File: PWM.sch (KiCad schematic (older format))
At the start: 28 parts

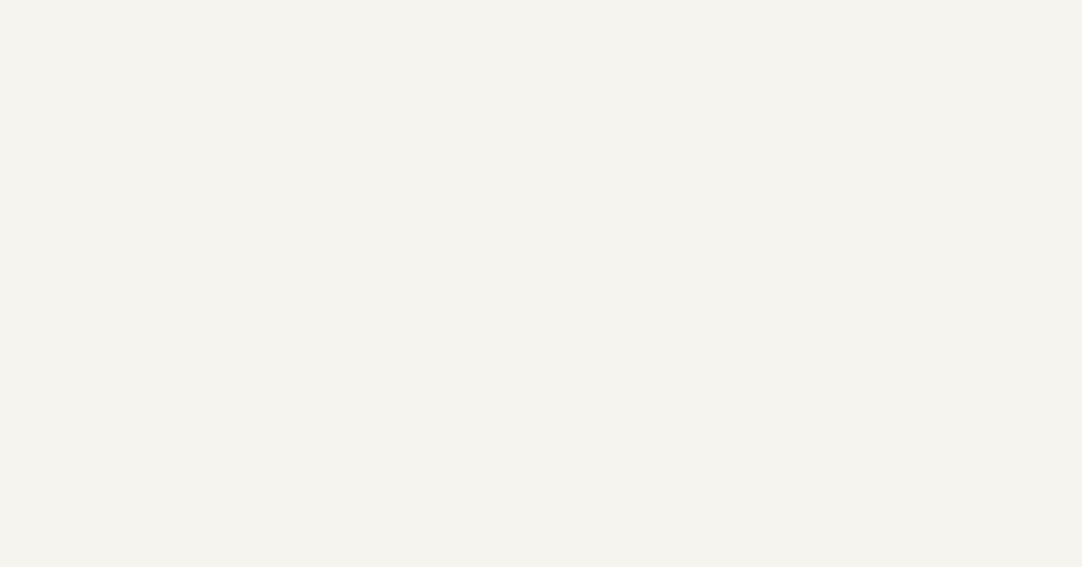
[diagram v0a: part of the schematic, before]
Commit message: added PWM
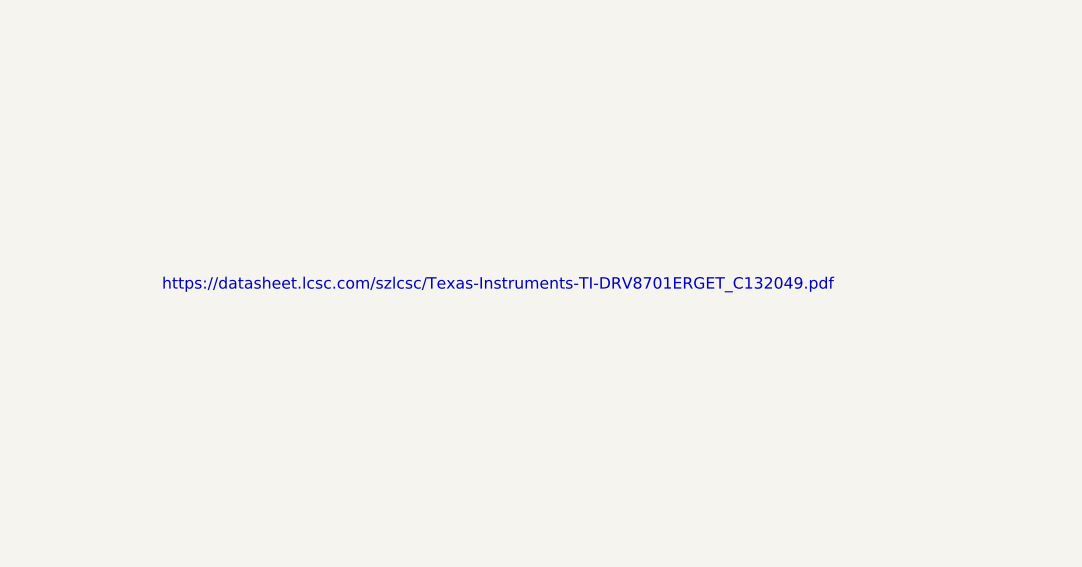
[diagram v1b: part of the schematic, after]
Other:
- note added: "https://datasheet.lcsc.com/szlcsc/Texas-Instruments-TI-DRV8701ERGET_C132049.pdf"
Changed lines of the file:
@@
 Wire Wire Line
 	1400 6300 1400 7200
+Text Notes 4650 6200 0    50   ~ 0
+https://datasheet.lcsc.com/szlcsc/Texas-Instruments-TI-DRV8701ERGET_C132049.pdf
 $EndSCHEMATC
